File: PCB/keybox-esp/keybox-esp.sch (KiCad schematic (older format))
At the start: 16 parts, among them J1 Micro_SD_Card, J2 USB_A, U1 ESP32-WROVER, U2 AP1117-50

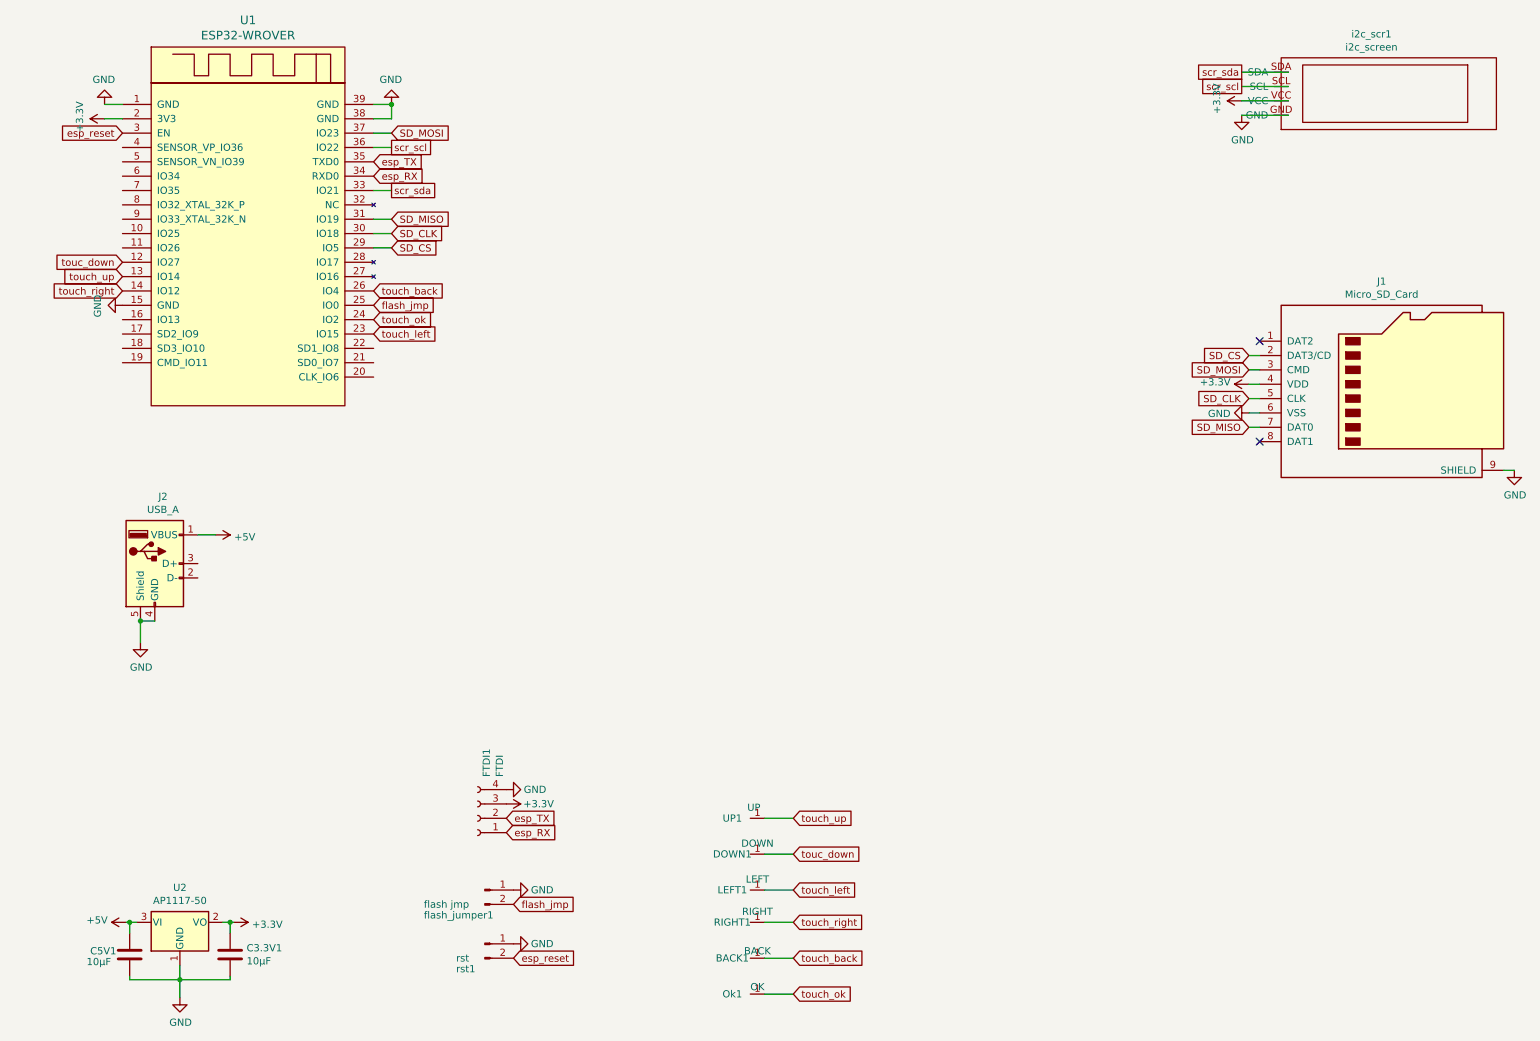
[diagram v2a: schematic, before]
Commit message: ajout de leds RGB
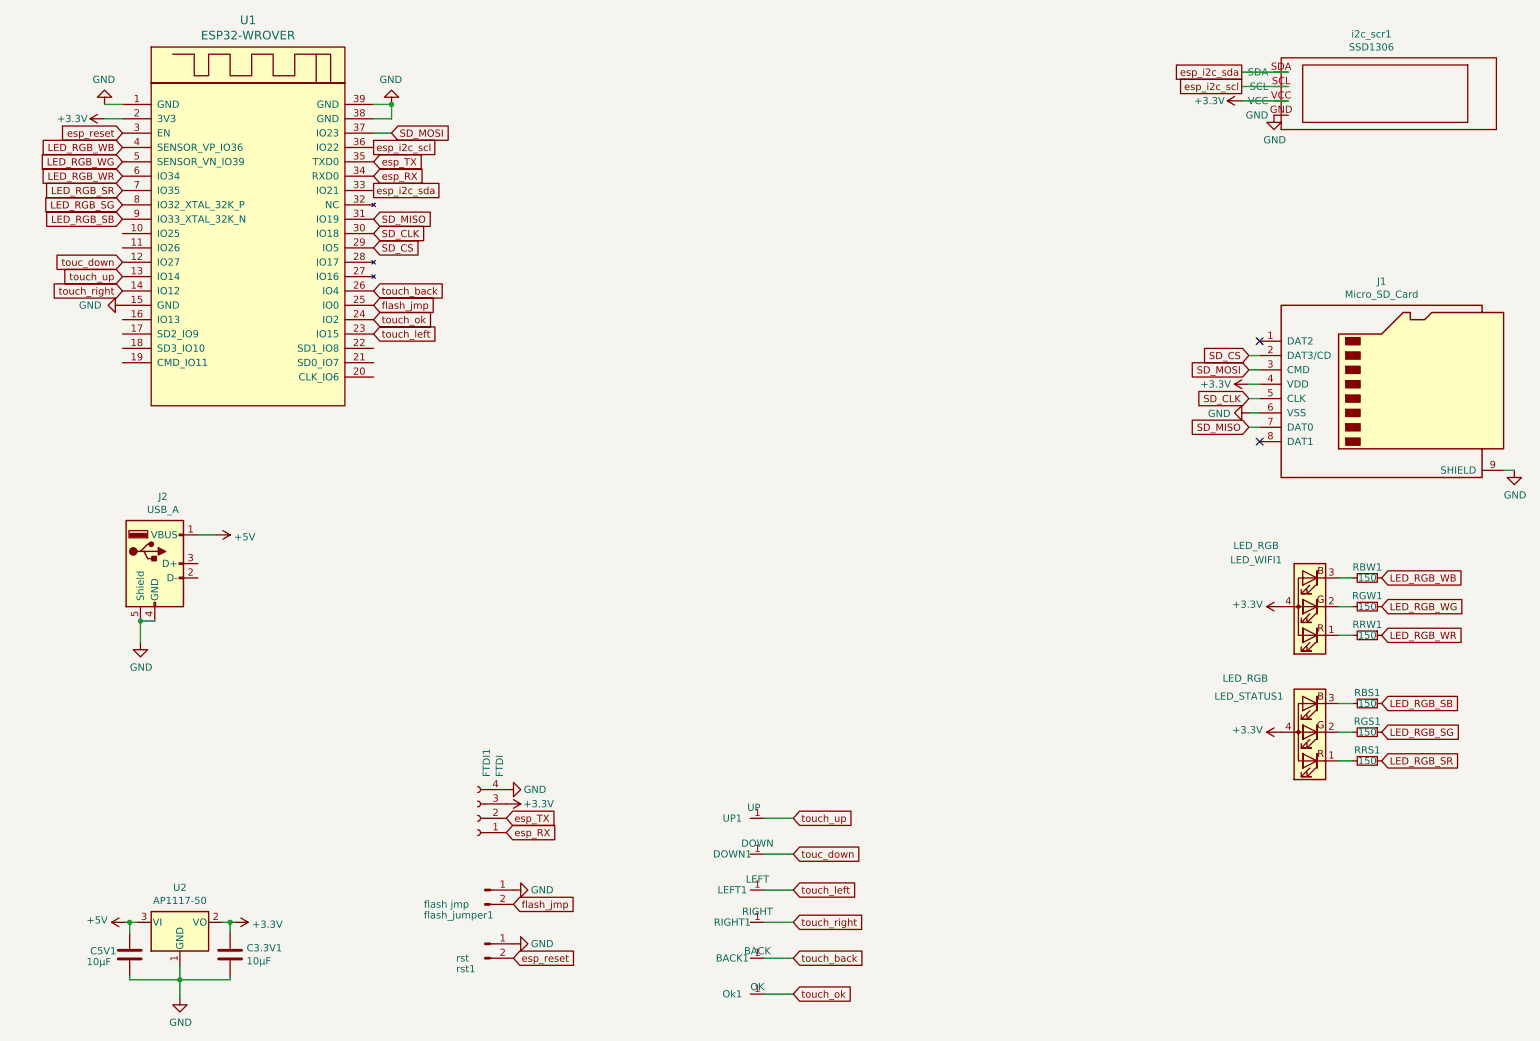
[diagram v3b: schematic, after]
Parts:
- added LED_STATUS1, LED_WIFI1: LED_RGB, LED_SMD:LED_Avago_PLCC4_3.2x2.8mm_CW, symbol Device:LED_RGBA
- added RBS1, RBW1, RGS1, RGW1, RRS1, RRW1: 150, Resistor_SMD:R_1206_3216Metric_Pad1.42x1.75mm_HandSolder, symbol Device:R_Small
- C3.3V1, C5V1: footprint AMS1117:C_1206_HandSoldering -> Capacitor_SMD:C_1206_3216Metric
- i2c_scr1: value i2c_screen -> SSD1306
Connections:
- net +3V3: now also LED_STATUS1.4 (A), LED_WIFI1.4 (A)
- net GND: no longer i2c_scr1.GND
- net LED_RGB_WB: now reaches U1.4 (SENSOR_VP_IO36)
- net LED_RGB_WB: now also RBW1.1
- net LED_RGB_WG: now reaches U1.5 (SENSOR_VN_IO39)
- net LED_RGB_WG: now also RGW1.1
- net LED_RGB_WR: now reaches U1.6 (IO34)
- net LED_RGB_WR: now also RRW1.1
- net LED_RGB_SR: now reaches U1.7 (IO35)
- net LED_RGB_SR: now also RRS1.1
- net LED_RGB_SG: now reaches U1.8 (IO32_XTAL_32K_P)
- net LED_RGB_SG: now also RGS1.1
- net LED_RGB_SB: now reaches U1.9 (IO33_XTAL_32K_N)
- net LED_RGB_SB: now also RBS1.1
- net scr_scl renamed esp_i2c_scl
- net scr_sda renamed esp_i2c_sda
- new net: LED_WIFI1.1 (RK), RRW1.2
- new net: LED_WIFI1.2 (GK), RGW1.2
- new net: LED_WIFI1.3 (BK), RBW1.2
- new net: LED_STATUS1.1 (RK), RRS1.2
- new net: LED_STATUS1.2 (GK), RGS1.2
- new net: LED_STATUS1.3 (BK), RBS1.2
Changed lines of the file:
@@
 P 9325 1500
 F 0 "i2c_scr1" H 9954 2165 50  0000 C CNN
-F 1 "i2c_screen" H 9954 2074 50  0000 C CNN
+F 1 "SSD1306" H 9954 2074 50  0000 C CNN
 F 2 "i2c_screen:i2c_screen" H 9725 1800 50  0001 C CNN
 F 3 "" H 9725 1800 50  0001 C CNN
@@
 P 9050 1300
 F 0 "#PWR0101" H 9050 1150 50  0001 C CNN
-F 1 "+3.3V" H 9065 1473 50  0000 C CNN
+F 1 "+3.3V" V 9050 1525 50  0000 C CNN
 F 2 "" H 9050 1300 50  0001 C CNN
 F 3 "" H 9050 1300 50  0001 C CNN
@@
 P 1125 1425
 F 0 "#PWR0102" H 1125 1275 50  0001 C CNN
-F 1 "+3.3V" H 1140 1598 50  0000 C CNN
+F 1 "+3.3V" V 1125 1650 50  0000 C CNN
 F 2 "" H 1125 1425 50  0001 C CNN
 F 3 "" H 1125 1425 50  0001 C CNN
@@
 L power:GND #PWR0103
 U 1 1 5E7273B8
-P 9050 1400
-F 0 "#PWR0103" H 9050 1150 50  0001 C CNN
-F 1 "GND" H 9055 1227 50  0000 C CNN
-F 2 "" H 9050 1400 50  0001 C CNN
-F 3 "" H 9050 1400 50  0001 C CNN
-	1    9050 1400
+P 9275 1400
+F 0 "#PWR0103" H 9275 1150 50  0001 C CNN
+F 1 "GND" H 9280 1227 50  0000 C CNN
+F 2 "" H 9275 1400 50  0001 C CNN
+F 3 "" H 9275 1400 50  0001 C CNN
+	1    9275 1400
 	1    0    0    -1
 $EndComp
@@
 P 1250 2725
 F 0 "#PWR0104" H 1250 2475 50  0001 C CNN
-F 1 "GND" H 1255 2552 50  0000 C CNN
+F 1 "GND" V 1250 2500 50  0000 C CNN
 F 2 "" H 1250 2725 50  0001 C CNN
 F 3 "" H 1250 2725 50  0001 C CNN
@@
 Wire Wire Line
 	1250 1325 1125 1325
-Text GLabel 3125 1625 2    50   UnSpc ~ 0
-scr_scl
-Text GLabel 3125 1925 2    50   UnSpc ~ 0
-scr_sda
+Text GLabel 3000 1625 2    50   UnSpc ~ 0
+esp_i2c_scl
+Text GLabel 3000 1925 2    50   UnSpc ~ 0
+esp_i2c_sda
 Text GLabel 9050 1200 0    50   UnSpc ~ 0
-scr_scl
+esp_i2c_scl
 Text GLabel 9050 1100 0    50   UnSpc ~ 0
-scr_sda
-Wire Wire Line
-	3000 1625 3125 1625
+esp_i2c_sda
 Wire Wire Line
 	3000 1525 3125 1525
@@
 Wire Wire Line
 	9375 1300 9050 1300
-Wire Wire Line
-	9375 1400 9050 1400
 $Comp
 L Connector:Micro_SD_Card J1
@@
 P 9100 3275
 F 0 "#PWR0108" H 9100 3125 50  0001 C CNN
-F 1 "+3.3V" V 9115 3403 50  0000 L CNN
+F 1 "+3.3V" V 9100 3400 50  0000 L CNN
 F 2 "" H 9100 3275 50  0001 C CNN
 F 3 "" H 9100 3275 50  0001 C CNN
@@
 Text GLabel 3125 1525 2    50   Input ~ 0
 SD_MOSI
-Wire Wire Line
-	3125 1925 3000 1925
-Text GLabel 3125 2325 2    50   Input ~ 0
+Text GLabel 3000 2325 2    50   Input ~ 0
 SD_CS
-Text GLabel 3125 2225 2    50   Input ~ 0
+Text GLabel 3000 2225 2    50   Input ~ 0
 SD_CLK
-Text GLabel 3125 2125 2    50   Input ~ 0
+Text GLabel 3000 2125 2    50   Input ~ 0
 SD_MISO
-Wire Wire Line
-	3125 2125 3000 2125
-Wire Wire Line
-	3000 2225 3125 2225
-Wire Wire Line
-	3125 2325 3000 2325
 $Comp
 L Connector:USB_A J2
@@
 F 0 "C3.3V1" H 2115 7296 50  0000 L CNN
 F 1 "10µF" H 2115 7205 50  0000 L CNN
-F 2 "AMS1117:C_1206_HandSoldering" H 2038 7100 50  0001 C CNN
+F 2 "Capacitor_SMD:C_1206_3216Metric" H 2038 7100 50  0001 C CNN
 F 3 "" H 2000 7250 50  0001 C CNN
 	1    2000 7250
@@
 F 0 "C5V1" H 1025 7275 50  0000 L CNN
 F 1 "10µF" H 1000 7200 50  0000 L CNN
-F 2 "AMS1117:C_1206_HandSoldering" H 1338 7100 50  0001 C CNN
+F 2 "Capacitor_SMD:C_1206_3216Metric" H 1338 7100 50  0001 C CNN
 F 3 "" H 1300 7250 50  0001 C CNN
 	1    1300 7250
@@
 Text GLabel 1250 2425 0    50   Input ~ 0
 touc_down
+$Comp
+L Device:LED_RGBA LED_STATUS1
+U 1 1 5E84A535
+P 9525 5700
+F 0 "LED_STATUS1" H 9950 5450 50  0000 C CNN
+F 1 "LED_RGB" H 9975 5325 50  0000 C CNN
+F 2 "LED_SMD:LED_Avago_PLCC4_3.2x2.8mm_CW" H 9525 5650 50  0001 C CNN
+F 3 "~" H 9525 5650 50  0001 C CNN
+	1    9525 5700
+	-1   0    0    1
+$EndComp
+$Comp
+L Device:R_Small RBW1
+U 1 1 5E85B7D2
+P 9925 4625
+F 0 "RBW1" V 9850 4625 50  0000 C CNN
+F 1 "150" V 9925 4625 50  0000 C CNN
+F 2 "Resistor_SMD:R_1206_3216Metric_Pad1.42x1.75mm_HandSolder" H 9925 4625 50  0001 C CNN
+F 3 "~" H 9925 4625 50  0001 C CNN
+	1    9925 4625
+	0    1    1    0
+$EndComp
+$Comp
+L Device:R_Small RGW1
+U 1 1 5E85DDCD
+P 9925 4825
+F 0 "RGW1" V 9850 4825 50  0000 C CNN
+F 1 "150" V 9925 4825 50  0000 C CNN
+F 2 "Resistor_SMD:R_1206_3216Metric_Pad1.42x1.75mm_HandSolder" H 9925 4825 50  0001 C CNN
+F 3 "~" H 9925 4825 50  0001 C CNN
+	1    9925 4825
+	0    1    1    0
+$EndComp
+$Comp
+L Device:R_Small RRW1
+U 1 1 5E85E879
+P 9925 5025
+F 0 "RRW1" V 9850 5025 50  0000 C CNN
+F 1 "150" V 9925 5025 50  0000 C CNN
+F 2 "Resistor_SMD:R_1206_3216Metric_Pad1.42x1.75mm_HandSolder" H 9925 5025 50  0001 C CNN
+F 3 "~" H 9925 5025 50  0001 C CNN
+	1    9925 5025
+	0    1    1    0
+$EndComp
+Wire Wire Line
+	9825 4625 9725 4625
+Wire Wire Line
+	9725 4825 9825 4825
+Wire Wire Line
+	9725 5025 9825 5025
+$Comp
+L Device:LED_RGBA LED_WIFI1
+U 1 1 5E8483AC
+P 9525 4825
+F 0 "LED_WIFI1" H 9900 4500 50  0000 C CNN
+F 1 "LED_RGB" H 9900 4400 50  0000 C CNN
+F 2 "LED_SMD:LED_Avago_PLCC4_3.2x2.8mm_CW" H 9525 4775 50  0001 C CNN
+F 3 "~" H 9525 4775 50  0001 C CNN
+	1    9525 4825
+	-1   0    0    1
+$EndComp
+$Comp
+L power:+3.3V #PWR0119
+U 1 1 5E877CDA
+P 9325 4825
+F 0 "#PWR0119" H 9325 4675 50  0001 C CNN
+F 1 "+3.3V" V 9340 4953 50  0000 L CNN
+F 2 "" H 9325 4825 50  0001 C CNN
+F 3 "" H 9325 4825 50  0001 C CNN
+	1    9325 4825
+	0    -1   -1   0
+$EndComp
+$Comp
+L power:+3.3V #PWR0120
+U 1 1 5E8780FE
+P 9325 5700
+F 0 "#PWR0120" H 9325 5550 50  0001 C CNN
+F 1 "+3.3V" V 9340 5828 50  0000 L CNN
+F 2 "" H 9325 5700 50  0001 C CNN
+F 3 "" H 9325 5700 50  0001 C CNN
+	1    9325 5700
+	0    -1   -1   0
+$EndComp
+$Comp
+L Device:R_Small RBS1
+U 1 1 5E882029
+P 9925 5500
+F 0 "RBS1" V 9850 5500 50  0000 C CNN
+F 1 "150" V 9925 5500 50  0000 C CNN
+F 2 "Resistor_SMD:R_1206_3216Metric_Pad1.42x1.75mm_HandSolder" H 9925 5500 50  0001 C CNN
+F 3 "~" H 9925 5500 50  0001 C CNN
+	1    9925 5500
+	0    1    1    0
+$EndComp
+$Comp
+L Device:R_Small RGS1
+U 1 1 5E88202F
+P 9925 5700
+F 0 "RGS1" V 9850 5700 50  0000 C CNN
+F 1 "150" V 9925 5700 50  0000 C CNN
+F 2 "Resistor_SMD:R_1206_3216Metric_Pad1.42x1.75mm_HandSolder" H 9925 5700 50  0001 C CNN
+F 3 "~" H 9925 5700 50  0001 C CNN
+	1    9925 5700
+	0    1    1    0
+$EndComp
+$Comp
+L Device:R_Small RRS1
+U 1 1 5E882035
+P 9925 5900
+F 0 "RRS1" V 9850 5900 50  0000 C CNN
+F 1 "150" V 9925 5900 50  0000 C CNN
+F 2 "Resistor_SMD:R_1206_3216Metric_Pad1.42x1.75mm_HandSolder" H 9925 5900 50  0001 C CNN
+F 3 "~" H 9925 5900 50  0001 C CNN
+	1    9925 5900
+	0    1    1    0
+$EndComp
+Wire Wire Line
+	9825 5500 9725 5500
+Wire Wire Line
+	9725 5700 9825 5700
+Wire Wire Line
+	9725 5900 9825 5900
+Text GLabel 10025 4625 2    50   Input ~ 0
+LED_RGB_WB
+Text GLabel 10025 4825 2    50   Input ~ 0
+LED_RGB_WG
+Text GLabel 10025 5025 2    50   Input ~ 0
+LED_RGB_WR
+Text GLabel 10025 5500 2    50   Input ~ 0
+LED_RGB_SB
+Text GLabel 10025 5700 2    50   Input ~ 0
+LED_RGB_SG
+Text GLabel 10025 5900 2    50   Input ~ 0
+LED_RGB_SR
+Text GLabel 1250 1625 0    50   Input ~ 0
+LED_RGB_WB
+Text GLabel 1250 1725 0    50   Input ~ 0
+LED_RGB_WG
+Text GLabel 1250 1825 0    50   Input ~ 0
+LED_RGB_WR
+Text GLabel 1250 1925 0    50   Input ~ 0
+LED_RGB_SR
+Text GLabel 1250 2025 0    50   Input ~ 0
+LED_RGB_SG
+Text GLabel 1250 2125 0    50   Input ~ 0
+LED_RGB_SB
 $EndSCHEMATC
